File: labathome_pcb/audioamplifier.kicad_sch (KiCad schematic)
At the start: 35 parts, among them J14 AUX OUT, J16 Headphones, J3 AUX IN, U10 NAU8822

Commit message: Minor improments on pcb
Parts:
- removed JP1: Jumper_2_Bridged, Jumper:SolderJumper-2_P1.3mm_Bridged2Bar_Pad1.0x1.5mm, symbol Jumper:Jumper_2_Bridged
- R23: footprint Diode_SMD:D_0805_2012Metric_Pad1.15x1.40mm_HandSolder -> Resistor_SMD:R_0805_2012Metric_Pad1.20x1.40mm_HandSolder; now fitted
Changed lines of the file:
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@@
-	)
-	(symbol
-		(lib_id "Jumper:Jumper_2_Bridged")
-		(at 39.37 88.9 0)
-		(unit 1)
-		(exclude_from_sim yes)
-		(in_bom yes)
-		(on_board yes)
-		(dnp no)
-		(fields_autoplaced yes)
-		(property "Reference" "JP1"
-			(at 39.37 83.82 0)
-			(effects
-				(font
-					(size 1.27 1.27)
-				)
-			)
-		)
-		(property "Value" "Jumper_2_Bridged"
-			(at 39.37 86.36 0)
-			(effects
-				(font
-					(size 1.27 1.27)
-				)
-			)
-		)
-		(property "Footprint" "Jumper:SolderJumper-2_P1.3mm_Bridged2Bar_Pad1.0x1.5mm"
-			(at 39.37 88.9 0)
-			(effects
-				(font
-					(size 1.27 1.27)
-				)
-				(hide yes)
-			)
-		)
-		(property "Datasheet" "~"
-			(at 39.37 88.9 0)
-			(effects
-				(font
-					(size 1.27 1.27)
-				)
-				(hide yes)
-			)
-		)
-		(property "Description" "Jumper, 2-pole, closed/bridged"
-			(at 39.37 88.9 0)
-			(effects
-				(font
-					(size 1.27 1.27)
-				)
-				(hide yes)
-			)
-		)
-		(pin "2"
-		)
-		(pin "1"
-		)
-		(instances
-			(project ""
-				(path "/e4d6926a-1a8b-424d-97c4-66b6ad87e4ac/2f2efef3-f887-4727-9b58-1fbd8d1c6d1d"
-					(reference "JP1")
-					(unit 1)
-				)
-			)
-		)
 	)
 	(symbol
@@
 		(in_bom yes)
 		(on_board yes)
-		(dnp yes)
+		(dnp no)
 		(property "Reference" "R23"
 			(at 38.1 89.408 90)
@@
 			)
 		)
-		(property "Footprint" "Diode_SMD:D_0805_2012Metric_Pad1.15x1.40mm_HandSolder"
+		(property "Footprint" "Resistor_SMD:R_0805_2012Metric_Pad1.20x1.40mm_HandSolder"
 			(at 38.1 93.218 90)
 			(effects

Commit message: Minor changes
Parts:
- C12, C13, C14, C15, C21, C22: MPN (none) -> CL05A475MP5NRNC; Manufacturer (none) -> Samsung Electro-Mechanics
- C16, C17, C20, C23, C24, C62: MPN (none) -> TAJA105K016RNJ; Manufacturer (none) -> Kyocera AVX
- C18, C19: MPN (none) -> RVE0J221M0605; Manufacturer (none) -> Honor Elec
- C65, C66: MPN (none) -> GRM033R61A104KE15D; Manufacturer (none) -> Murata Electronics
- FB1: MPN (none) -> BLM18AG601SN1D; Manufacturer (none) -> Murata Electronics
- J14, J16, J3: MPN (none) -> PJ-327A0-SMT; Manufacturer (none) -> XKB Connection
- MK1: MPN (none) -> GMI6050P-64DB; Manufacturer (none) -> INGHAi
- R23: MPN (none) -> 0805W8F0000T5E; Manufacturer (none) -> UNI-ROYAL(Uniroyal Elec)
- R24: MPN (none) -> 0402WGF2201TCE; Manufacturer (none) -> UNI-ROYAL(Uniroyal Elec)
- R25, R54: MPN (none) -> 0201WMF1003TEE; Manufacturer (none) -> UNI-ROYAL(Uniroyal Elec)
- R26, R27, R55: MPN (none) -> 0201WMF1002TEE; Manufacturer (none) -> UNI-ROYAL(Uniroyal Elec)
- U10: MPN (none) -> NAU88C22YG; Manufacturer (none) -> Nuvoton Tech

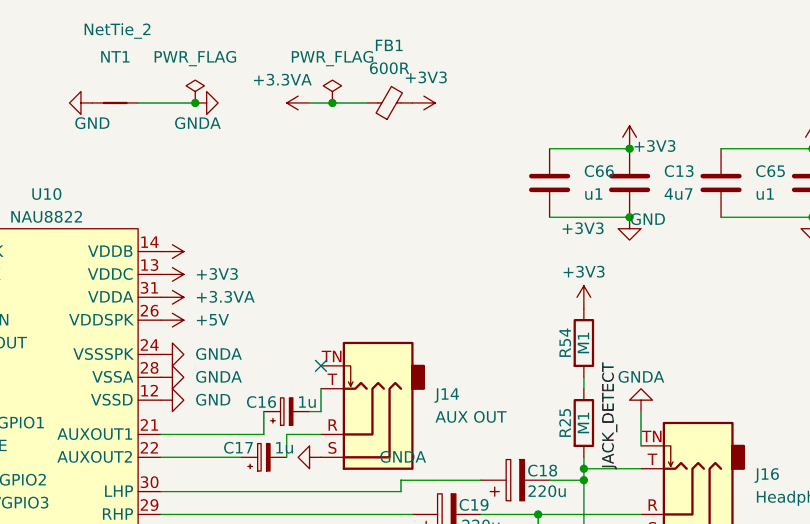
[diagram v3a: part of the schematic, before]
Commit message: Labathome PCB -> KICAD 9
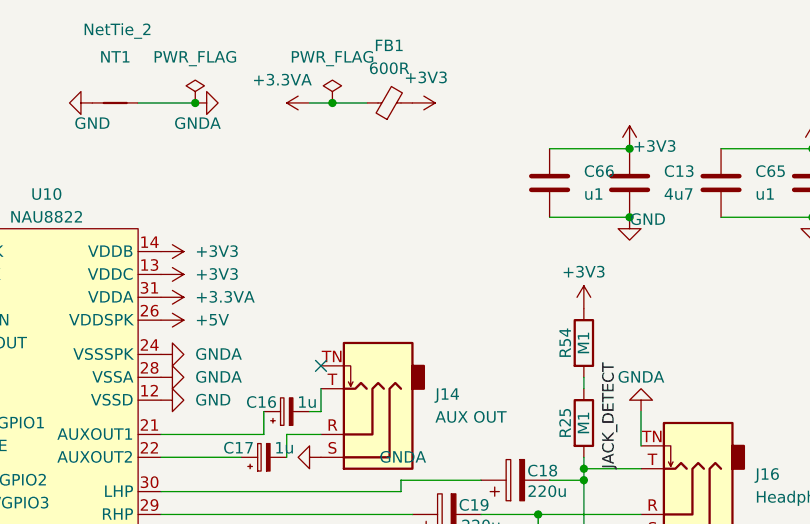
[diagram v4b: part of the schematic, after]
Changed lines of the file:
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@@
 (kicad_sch
-	(version 20231120)
+	(version 20250114)
 	(generator "eeschema")
-	(generator_version "8.0")
+	(generator_version "9.0")
 	(paper "A4")
 	(title_block
@@
 		)
 		(property "Value" "+3V3"
-			(at 144.78 50.7999 90)
-			(effects
-				(font
+			(at 104.14 53.34 90)
+			(effects
+				(font
